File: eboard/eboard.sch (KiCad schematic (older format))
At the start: 81 parts, among them J1 Conn_01x02_Male, J2 USB_B_Micro, J3 Conn_01x03_Male, J4 jst_battery, J5 Conn_01x02_Male, J6 Conn_01x03_Male, Q1 AO4407, Q2 S8050, Q3 S8050, Q6 AO4407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

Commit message: ecos from v1
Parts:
- H1, H2, H3, H4: value MountingHole -> MountingHole_Pad; footprint MountingHole:MountingHole_3.2mm_M3 -> MountingHole:MountingHole_3.2mm_M3_Pad
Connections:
- net RXD: now also U5.26 (TXD); no longer U5.25 (RXD)
- net TXD: now also U5.25 (RXD); no longer U5.26 (TXD)
- net Vraw: now also R5.1, U2.6 (EN), U2.7 (PS/SYNC), U2.8 (VINA)
- net Vraw_for_5v: now also R9.1, U6.6 (EN), U6.7 (PS/SYNC), U6.8 (VINA)
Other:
- note added: "TX/RX reversed\non purpose"
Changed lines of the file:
@@
 $EndComp
 Wire Wire Line
-	1800 4650 1100 4650
+	1800 4650 1450 4650
 Wire Wire Line
 	1100 4650 1100 4850
@@
 Text GLabel 9650 1800 2    50   Input ~ 0
 BOOT0
-Text GLabel 7000 5750 2    50   Input ~ 0
+Text GLabel 7000 5650 2    50   Input ~ 0
 RXD
 Text GLabel 7000 5850 2    50   Input ~ 0
 RTS
-Text GLabel 7000 5650 2    50   Input ~ 0
+Text GLabel 7000 5750 2    50   Input ~ 0
 TXD
 Wire Wire Line
@@
 Wire Wire Line
 	2100 900  1900 900
-$Comp
-L pace:PWR_FLAG #FLG?
-U 1 1 5FE5E012
-P 1450 4550
-F 0 "#FLG?" H 1450 4625 50  0001 C CNN
-F 1 "PWR_FLAG" H 1450 4723 50  0001 C CNN
-F 2 "" H 1450 4550 50  0001 C CNN
-F 3 "~" H 1450 4550 50  0001 C CNN
-	1    1450 4550
-	1    0    0    -1
-$EndComp
-Wire Wire Line
-	1450 4750 1450 4550
+Wire Wire Line
+	1450 4750 1450 4650
 Connection ~ 1450 4750
 Wire Wire Line
-	1050 6800 1750 6800
+	1050 6800 1400 6800
 NoConn ~ 4000 1500
 NoConn ~ 5000 1300
@@
 Connection ~ 1400 6900
 Wire Wire Line
-	1400 6750 1400 6900
-$Comp
-L pace:PWR_FLAG #FLG?
-U 1 1 5FE6C363
-P 1400 6750
-F 0 "#FLG?" H 1400 6825 50  0001 C CNN
-F 1 "PWR_FLAG" H 1400 6923 50  0001 C CNN
-F 2 "" H 1400 6750 50  0001 C CNN
-F 3 "~" H 1400 6750 50  0001 C CNN
-	1    1400 6750
-	1    0    0    -1
-$EndComp
+	1400 6800 1400 6900
 Text GLabel 950  6800 0    50   Input ~ 0
 Vraw_for_5v
@@
 P 6050 1050
 F 0 "H1" H 6150 1050 50  0000 L CNN
-F 1 "MountingHole" H 6150 1005 50  0001 L CNN
-F 2 "MountingHole:MountingHole_3.2mm_M3" H 6050 1050 50  0001 C CNN
+F 1 "MountingHole_Pad" H 6150 1005 50  0001 L CNN
+F 2 "MountingHole:MountingHole_3.2mm_M3_Pad" H 6050 1050 50  0001 C CNN
 F 3 "~" H 6050 1050 50  0001 C CNN
 	1    6050 1050
@@
 P 6650 1050
 F 0 "H3" H 6750 1050 50  0000 L CNN
-F 1 "MountingHole" H 6750 1005 50  0001 L CNN
-F 2 "MountingHole:MountingHole_3.2mm_M3" H 6650 1050 50  0001 C CNN
+F 1 "MountingHole_Pad" H 6750 1005 50  0001 L CNN
+F 2 "MountingHole:MountingHole_3.2mm_M3_Pad" H 6650 1050 50  0001 C CNN
 F 3 "~" H 6650 1050 50  0001 C CNN
 	1    6650 1050
@@
 P 6350 1050
 F 0 "H2" H 6450 1050 50  0000 L CNN
-F 1 "MountingHole" H 6450 1005 50  0001 L CNN
-F 2 "MountingHole:MountingHole_3.2mm_M3" H 6350 1050 50  0001 C CNN
+F 1 "MountingHole_Pad" H 6450 1005 50  0001 L CNN
+F 2 "MountingHole:MountingHole_3.2mm_M3_Pad" H 6350 1050 50  0001 C CNN
 F 3 "~" H 6350 1050 50  0001 C CNN
 	1    6350 1050
@@
 P 6950 1050
 F 0 "H4" H 7050 1050 50  0000 L CNN
-F 1 "MountingHole" H 7050 1005 50  0001 L CNN
-F 2 "MountingHole:MountingHole_3.2mm_M3" H 6950 1050 50  0001 C CNN
+F 1 "MountingHole_Pad" H 7050 1005 50  0001 L CNN
+F 2 "MountingHole:MountingHole_3.2mm_M3_Pad" H 6950 1050 50  0001 C CNN
 F 3 "~" H 6950 1050 50  0001 C CNN
 	1    6950 1050
@@
 $EndComp
 Connection ~ 6050 1150
+Connection ~ 1450 4650
+Wire Wire Line
+	1450 4650 1100 4650
+Connection ~ 1400 6800
+Wire Wire Line
+	1400 6800 1750 6800
+Text Notes 7300 5750 0    50   ~ 0
+TX/RX reversed\non purpose
 $EndSCHEMATC

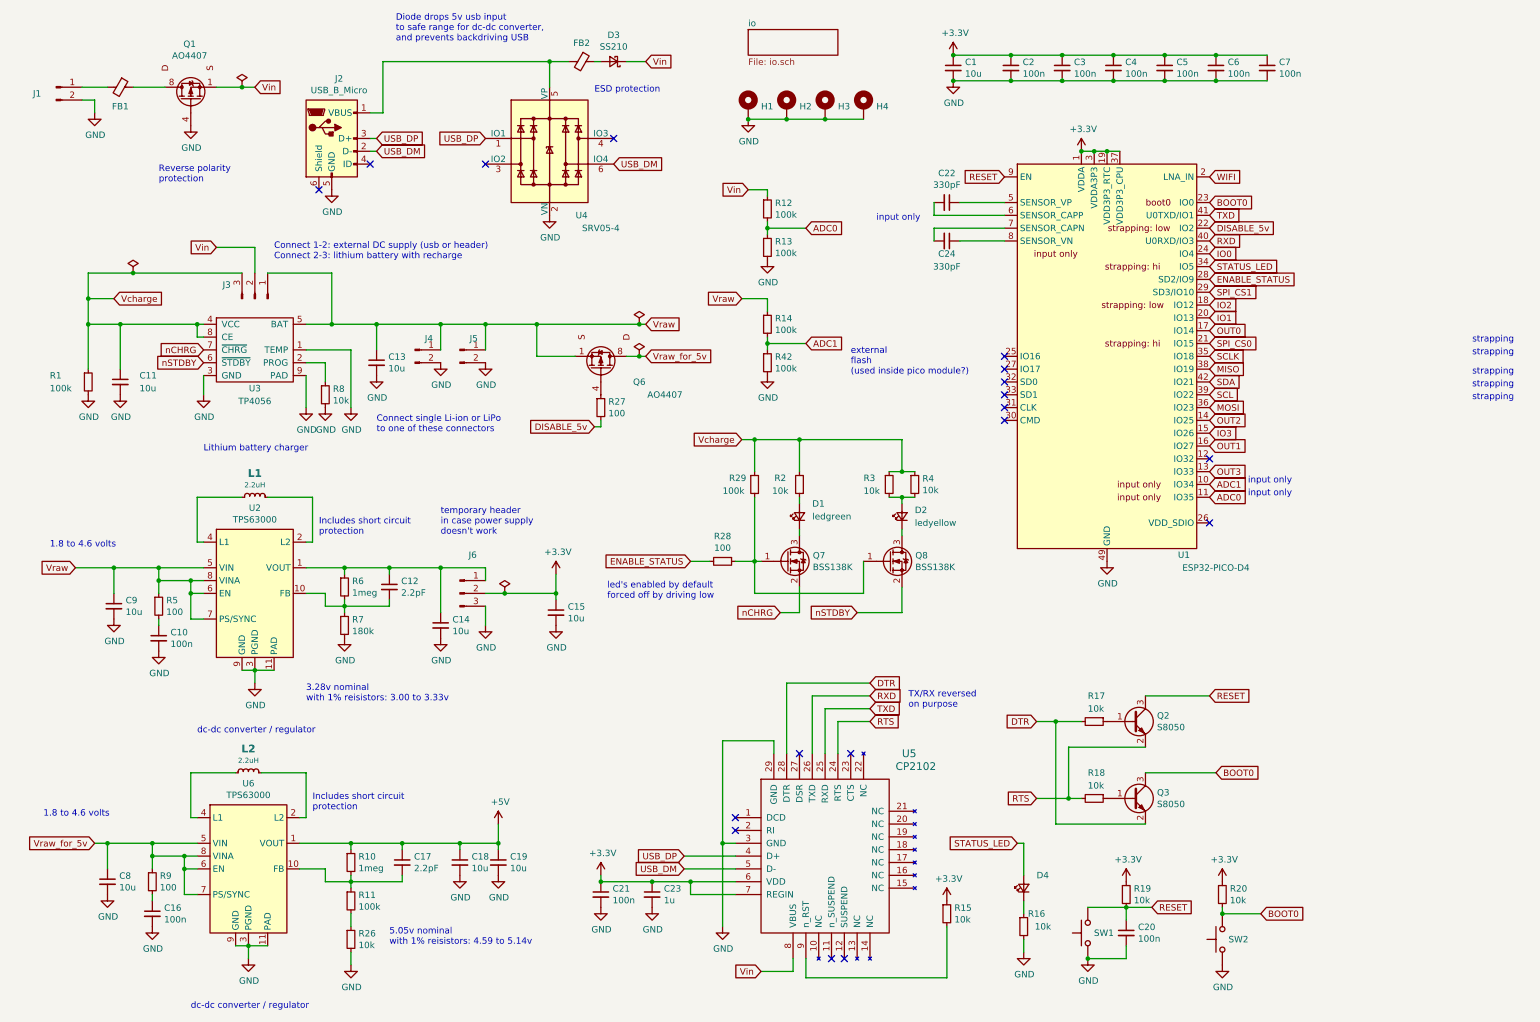
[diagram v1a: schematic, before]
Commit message: remove 5v
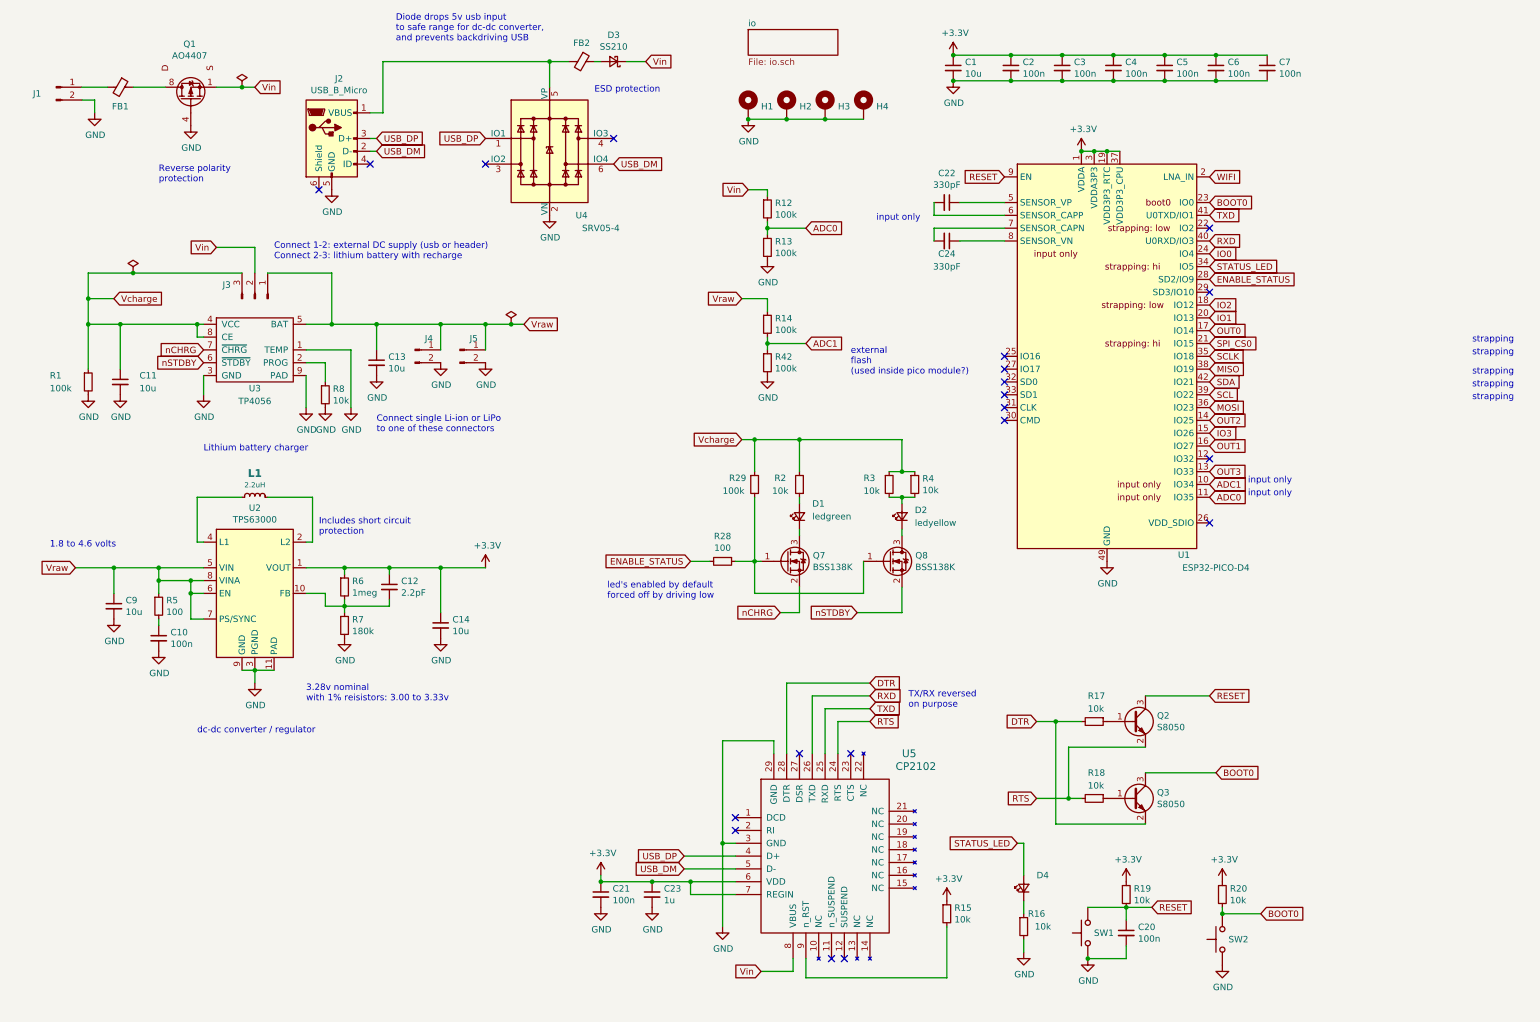
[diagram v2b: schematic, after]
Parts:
- removed C15, C18, C19, C8: 10u, Capacitor_SMD:C_0402_1005Metric, symbol pace:10u
- removed C16: 100n, Capacitor_SMD:C_0402_1005Metric, symbol pace:100n
- removed C17: 2.2pF, Capacitor_SMD:C_0402_1005Metric, symbol pace:2.2pF
- removed J6: Conn_01x03_Male, Connector_PinHeader_2.54mm:PinHeader_1x03_P2.54mm_Vertical, symbol pace:Conn_01x03_Male
- removed L2: 2.2uH, Inductor_SMD:L_Coilcraft_XxL4020, symbol pace:2.2uH
- removed Q6: AO4407, Package_SO:SOIC-8_3.9x4.9mm_P1.27mm, symbol pace:AO4407
- removed R10: 1meg, Resistor_SMD:R_0603_1608Metric, symbol pace:1meg
- removed R11: 100k, Resistor_SMD:R_0402_1005Metric, symbol pace:100k
- removed R26: 10k, Resistor_SMD:R_0402_1005Metric, symbol pace:10k
- removed R27, R9: 100, Resistor_SMD:R_0402_1005Metric, symbol pace:100
- removed U6: TPS63000, Package_SON:Texas_DRC0010J_ThermalVias, symbol pace:TPS63000
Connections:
- net +3V3: now also C12.1, C14.1, R6.1, U2.1 (VOUT)
- net DISABLE_5v: no longer names the net of U1.22 (IO2)
- net SPI_CS1: no longer names the net of U1.29 (SD3/IO10)
- no-connect marks 18 -> 20
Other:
- note removed: "5.05v nominal\nwith 1% reisistors: 4.59 to 5.14v"
- note removed: "temporary header\nin case power supply\ndoesn't work\n"

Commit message: v2
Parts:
- removed Q7, Q8: BSS138K, Package_TO_SOT_SMD:SOT-23, symbol pace:BSS138K
- removed R28: 100, Resistor_SMD:R_0402_1005Metric, symbol pace:100
- removed R29: 100k, Resistor_SMD:R_0402_1005Metric, symbol pace:100k
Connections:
- net nCHRG: now also D1.1 (K)
- net nSTDBY: now also D2.1 (K)
- net ENABLE_STATUS: no longer names the net of U1.28 (SD2/IO9)
- no-connect marks 20 -> 21
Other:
- note removed: "led's enabled by default\nforced off by driving low"
- note removed: "strapping"
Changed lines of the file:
@@
 	1    0    0    -1
 $EndComp
-Text GLabel 4300 2750 2    50   Input ~ 0
-Vraw
-Wire Wire Line
-	4300 2750 4200 2750
-Connection ~ 4000 2750
 $Comp
 L pace:Conn_01x03_Male J3
@@
 P 8200 7150
 F 0 "D4" V 8300 7050 50  0000 R CNN
-F 1 "ledgreen" V 7850 7250 50  0001 R CNN
+F 1 "ledgreen" V 8200 7050 50  0000 R CNN
 F 2 "LED_SMD:LED_0603_1608Metric" V 8200 7150 50  0001 C CNN
 F 3 "https://lcsc.com/product-detail/Light-Emitting-Diodes-LED_Green-0805-Iv-207-249-mcd-atIF-20mA_C2297.html/?href=jlc-SMT" V 8200 7150 50  0001 C CNN
@@
 Text Notes 3300 550  0    50   ~ 0
 Diode drops 5v usb input\nto safe range for dc-dc converter,\nand prevents backdriving USB
-Text GLabel 5600 4600 0    50   Input ~ 0
-ENABLE_STATUS
 Wire Wire Line
 	1900 2150 2200 2150
@@
 Wire Wire Line
 	7250 4100 7250 4150
-Wire Wire Line
-	7250 4350 7250 4400
-$Comp
-L pace:100k R29
-U 1 1 5FF35D92
-P 6100 4000
-F 0 "R29" H 5900 4050 50  0000 L CNN
-F 1 "100k" H 5850 3950 50  0000 L CNN
-F 2 "Resistor_SMD:R_0402_1005Metric" H 6100 4000 50  0001 C CNN
-F 3 "https://datasheet.lcsc.com/szlcsc/Uniroyal-Elec-0402WGF1002TCE_C25744.pdf" H 6100 4000 50  0001 C CNN
-F 4 "C25741" H 6100 4000 50  0001 C CNN "LCSC"
-	1    6100 4000
-	1    0    0    -1
-$EndComp
-Text Notes 4950 4900 0    50   ~ 0
-led's enabled by default\nforced off by driving low
-$Comp
-L pace:100 R28
-U 1 1 60077714
-P 5850 4600
-F 0 "R28" V 5654 4600 50  0000 C CNN
-F 1 "100" V 5745 4600 50  0000 C CNN
-F 2 "Resistor_SMD:R_0402_1005Metric" H 5850 4600 50  0001 C CNN
-F 3 "https://datasheet.lcsc.com/szlcsc/Uniroyal-Elec-0402WGF1002TCE_C25744.pdf" H 5850 4600 50  0001 C CNN
-F 4 "C25076" H 5850 4600 50  0001 C CNN "LCSC"
-	1    5850 4600
-	0    1    1    0
-$EndComp
-Wire Wire Line
-	5600 4600 5750 4600
 Text GLabel 1800 2950 0    50   Input ~ 0
 nCHRG
@@
 Connection ~ 1150 2750
 Connection ~ 900  2750
-$Comp
-L pace:PWR_FLAG #FLG?
-U 1 1 60179862
-P 4200 2750
-F 0 "#FLG?" H 4200 2825 50  0001 C CNN
-F 1 "PWR_FLAG" H 4200 2923 50  0001 C CNN
-F 2 "" H 4200 2750 50  0001 C CNN
-F 3 "~" H 4200 2750 50  0001 C CNN
-	1    4200 2750
-	1    0    0    -1
-$EndComp
-Connection ~ 4200 2750
 Text GLabel 1100 2550 2    50   Input ~ 0
 Vcharge
@@
 Vcharge
 Wire Wire Line
-	6000 3650 6100 3650
-Wire Wire Line
 	6450 3650 6450 3900
-Wire Wire Line
-	5950 4600 6100 4600
-Text GLabel 6300 5000 0    50   Input ~ 0
+Text GLabel 6300 4600 0    50   Input ~ 0
 nCHRG
 Wire Wire Line
-	6450 5000 6450 4800
-Wire Wire Line
-	6300 5000 6450 5000
-Wire Wire Line
-	6100 3650 6100 3900
-Connection ~ 6100 3650
-Wire Wire Line
-	6100 3650 6450 3650
-Wire Wire Line
-	6100 4100 6100 4600
-Connection ~ 6100 4600
-Wire Wire Line
-	6100 4600 6150 4600
+	6300 4600 6450 4600
 Wire Wire Line
 	7150 3900 7250 3900
-Text GLabel 6900 5000 0    50   Input ~ 0
+Text GLabel 6900 4600 0    50   Input ~ 0
 nSTDBY
 Wire Wire Line
-	6900 5000 7250 5000
-Wire Wire Line
-	7250 5000 7250 4800
-Wire Wire Line
-	6100 4600 6100 4850
-Wire Wire Line
-	6100 4850 6950 4850
-Wire Wire Line
-	6950 4850 6950 4600
+	6900 4600 7250 4600
 Wire Wire Line
 	6450 3650 7250 3650
@@
 Wire Wire Line
 	6450 4150 6450 4100
-Wire Wire Line
-	6450 4400 6450 4350
-Text GLabel 9650 2400 2    50   Input ~ 0
-ENABLE_STATUS
 Connection ~ 3250 4650
 Text GLabel 9650 1600 2    50   Input ~ 0
 WIFI
-$Comp
-L pace:BSS138K Q7
-U 1 1 5FD52255
-P 6350 4600
-F 0 "Q7" H 6554 4646 50  0000 L CNN
-F 1 "BSS138K" H 6554 4555 50  0000 L CNN
-F 2 "Package_TO_SOT_SMD:SOT-23" H 6550 4700 50  0001 C CNN
-F 3 "http://www.st.com/st-web-ui/static/active/en/resource/technical/document/datasheet/CD00000544.pdf" H 6350 4600 50  0001 C CNN
-F 4 "C255592" H 6350 4600 50  0001 C CNN "LCSC"
-	1    6350 4600
-	1    0    0    -1
-$EndComp
-$Comp
-L pace:BSS138K Q8
-U 1 1 5FD52A2E
-P 7150 4600
-F 0 "Q8" H 7354 4646 50  0000 L CNN
-F 1 "BSS138K" H 7354 4555 50  0000 L CNN
-F 2 "Package_TO_SOT_SMD:SOT-23" H 7350 4700 50  0001 C CNN
-F 3 "http://www.st.com/st-web-ui/static/active/en/resource/technical/document/datasheet/CD00000544.pdf" H 7150 4600 50  0001 C CNN
-F 4 "C255592" H 7150 4600 50  0001 C CNN "LCSC"
-	1    7150 4600
-	1    0    0    -1
-$EndComp
 $Comp
 L pace:PWR_FLAG #FLG?
@@
 Wire Wire Line
 	6200 2900 6200 2950
-Text Notes 11700 3150 0    50   ~ 0
-strapping
-Text Notes 11700 3250 0    50   ~ 0
-strapping
-Text Notes 11700 3350 0    50   ~ 0
-strapping
-Text Notes 11700 3000 0    50   ~ 0
-strapping
-Text Notes 11700 2900 0    50   ~ 0
-strapping
 Text GLabel 9650 2700 2    50   Input ~ 0
 IO1
@@
 NoConn ~ 9650 2000
 Wire Wire Line
-	4000 2750 4200 2750
-Wire Wire Line
 	2900 4650 3250 4650
 NoConn ~ 9650 2500
+Wire Wire Line
+	6000 3650 6450 3650
+Wire Wire Line
+	7250 4350 7250 4600
+Wire Wire Line
+	6450 4350 6450 4600
+Connection ~ 4000 2750
+Wire Wire Line
+	4000 2750 4200 2750
+Connection ~ 4200 2750
+$Comp
+L pace:PWR_FLAG #FLG?
+U 1 1 60179862
+P 4200 2750
+F 0 "#FLG?" H 4200 2825 50  0001 C CNN
+F 1 "PWR_FLAG" H 4200 2923 50  0001 C CNN
+F 2 "" H 4200 2750 50  0001 C CNN
+F 3 "~" H 4200 2750 50  0001 C CNN
+	1    4200 2750
+	1    0    0    -1
+$EndComp
+Wire Wire Line
+	4300 2750 4200 2750
+Text GLabel 4300 2750 2    50   Input ~ 0
+Vraw
+NoConn ~ 9650 2400
 $EndSCHEMATC

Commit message: v2a
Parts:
- Q1: LCSC C16072 -> C469397
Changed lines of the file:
@@
 F 2 "Package_SO:SOIC-8_3.9x4.9mm_P1.27mm" H 1900 1100 50  0001 C CNN
 F 3 "https://jlcpcb.com/parts/componentSearch?searchTxt=ao4407" H 1700 1000 50  0001 C CNN
-F 4 "C16072" H 1700 1000 50  0001 C CNN "LCSC"
+F 4 "C469397" H 1700 1000 50  0001 C CNN "LCSC"
 	1    1700 1000
 	0    -1   -1   0

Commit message: leds
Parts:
- removed D1, D4: ledgreen, LED_SMD:LED_0603_1608Metric, symbol pace:ledgreen
- added D1: ledgreen_0805, LED_SMD:LED_0805_2012Metric, symbol pace:ledgreen_0805
- added D4: ledyellow, LED_SMD:LED_0603_1608Metric, symbol pace:ledyellow
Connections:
- net STATUS_LED: now also D4.2 (A)
- net nCHRG: now also D1.1 (K)
- net at R2.1: now also D1.2 (A)
- net at R16.1: now also D4.1 (K)
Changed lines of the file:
@@
 Connect single Li-ion or LiPo\nto one of these connectors
-$Comp
-L pace:ledgreen D1
-U 1 1 5FCA0A0E
-P 6450 4250
-F 0 "D1" V 6550 4150 50  0000 R CNN
-F 1 "ledgreen" V 6450 4150 50  0000 R CNN
-F 2 "LED_SMD:LED_0603_1608Metric" V 6450 4250 50  0001 C CNN
-F 3 "https://lcsc.com/product-detail/Light-Emitting-Diodes-LED_Green-0805-Iv-207-249-mcd-atIF-20mA_C2297.html/?href=jlc-SMT" V 6450 4250 50  0001 C CNN
-F 4 "C2297" H 6450 4250 50  0001 C CNN "LCSC"
-	1    6450 4250
-	0    -1   -1   0
-$EndComp
 $Comp
 L pace:10k R4
@@
 Text GLabel 8050 1600 0    50   Input ~ 0
 RESET
-$Comp
-L pace:ledgreen D4
-U 1 1 5FB8D839
-P 8200 7150
-F 0 "D4" V 8300 7050 50  0000 R CNN
-F 1 "ledgreen" V 8200 7050 50  0000 R CNN
-F 2 "LED_SMD:LED_0603_1608Metric" V 8200 7150 50  0001 C CNN
-F 3 "https://lcsc.com/product-detail/Light-Emitting-Diodes-LED_Green-0805-Iv-207-249-mcd-atIF-20mA_C2297.html/?href=jlc-SMT" V 8200 7150 50  0001 C CNN
-F 4 "C2297" H 8200 7150 50  0001 C CNN "LCSC"
-	1    8200 7150
-	0    -1   -1   0
-$EndComp
 Text GLabel 8150 6800 0    50   Input ~ 0
 STATUS_LED
@@
 Vraw
 NoConn ~ 9650 2400
+$Comp
+L pace:ledgreen_0805 D1
+U 1 1 603C8290
+P 6450 4250
+F 0 "D1" V 6496 4180 50  0000 R CNN
+F 1 "ledgreen_0805" V 6405 4180 50  0000 R CNN
+F 2 "LED_SMD:LED_0805_2012Metric" V 6450 4250 50  0001 C CNN
+F 3 "https://lcsc.com/product-detail/Light-Emitting-Diodes-LED_Green-0805-Iv-207-249-mcd-atIF-20mA_C2297.html/?href=jlc-SMT" V 6450 4250 50  0001 C CNN
+F 4 "C2297" H 6450 4250 50  0001 C CNN "LCSC"
+	1    6450 4250
+	0    -1   -1   0
+$EndComp
+$Comp
+L pace:ledyellow D4
+U 1 1 603E7730
+P 8200 7150
+F 0 "D4" V 8246 7080 50  0000 R CNN
+F 1 "ledyellow" V 8155 7080 50  0000 R CNN
+F 2 "LED_SMD:LED_0603_1608Metric" V 8200 7150 50  0001 C CNN
+F 3 "https://lcsc.com/product-detail/Light-Emitting-Diodes-LED_0603-Yellow-light_C72038.html/?href=jlc-SMT" V 8200 7150 50  0001 C CNN
+F 4 "C72038" H 8200 7150 50  0001 C CNN "LCSC"
+	1    8200 7150
+	0    -1   -1   0
+$EndComp
 $EndSCHEMATC
